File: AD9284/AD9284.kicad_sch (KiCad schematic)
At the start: 0 parts

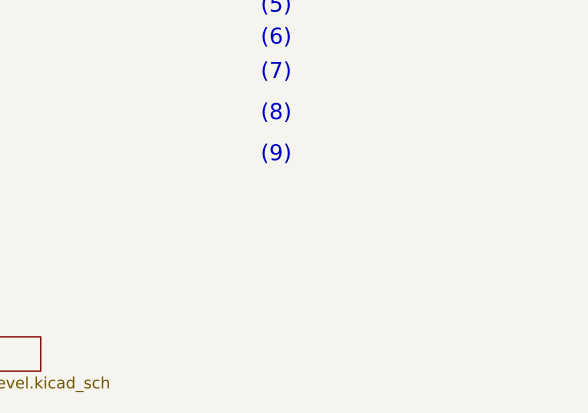
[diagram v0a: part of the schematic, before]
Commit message: Schematic and PCB complete. TODO: BOM
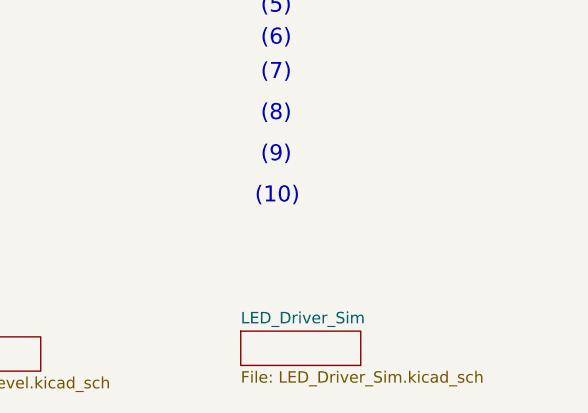
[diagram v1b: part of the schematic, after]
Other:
- added sheet LED_Driver_Sim (LED_Driver_Sim.kicad_sch)
- note added: "(10)"
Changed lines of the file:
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@@
+		)
+	)
+	(text "(10)"
+		(exclude_from_sim no)
+		(at 193.294 120.904 0)
+		(effects
+			(font
+				(size 1.778 1.778)
+			)
+			(href "#10")
 		)
 	)
@@
 		)
 		(column_widths 6.35 86.995 17.399)
-		(row_heights 3.81 3.81 3.81 3.81 3.81 3.81 3.81 4.572 4.572)
+		(row_heights 3.81 3.81 3.81 3.81 3.81 3.81 3.81 4.572 4.572 4.572)
 		(cells
 			(table_cell "1"
@@
 				)
 			)
-			(table_cell "References"
+			(table_cell "LED bjt driver sim"
 				(exclude_from_sim no)
 				(at 97.79 113.792 0)
@@
 				(exclude_from_sim no)
 				(at 184.785 113.792 0)
+				(size 17.399 4.572)
+				(margins 0.9525 0.9525 0.9525 0.9525)
+				(span 1 1)
+				(fill
+					(type none)
+				)
+				(effects
+					(font
+						(size 2.032 2.032)
+					)
+					(justify left top)
+				)
+			)
+			(table_cell "10"
+				(exclude_from_sim no)
+				(at 91.44 118.364 0)
+				(size 6.35 4.572)
+				(margins 0.9525 0.9525 0.9525 0.9525)
+				(span 1 1)
+				(fill
+					(type none)
+				)
+				(effects
+					(font
+						(size 2.032 2.032)
+					)
+					(justify left top)
+				)
+			)
+			(table_cell "References"
+				(exclude_from_sim no)
+				(at 97.79 118.364 0)
+				(size 86.995 4.572)
+				(margins 0.9525 0.9525 0.9525 0.9525)
+				(span 1 1)
+				(fill
+					(type none)
+				)
+				(effects
+					(font
+						(size 2.032 2.032)
+					)
+					(justify left top)
+				)
+			)
+			(table_cell ""
+				(exclude_from_sim no)
+				(at 184.785 118.364 0)
 				(size 17.399 4.572)
 				(margins 0.9525 0.9525 0.9525 0.9525)
@@
 			(effects
 				(font
+					(size 1.27 1.27)
+				)
+				(justify left top)
+			)
+		)
+		(instances
+			(project "AD9284"
+				(path "/d7c6bdb5-efe4-402d-982f-a101ad564d95"
+					(page "10")
+				)
+			)
+		)
+	)
+	(sheet
+		(at 189.23 135.89)
+		(size 13.335 3.81)
+		(exclude_from_sim no)
+		(in_bom yes)
+		(on_board yes)
+		(dnp no)
+		(fields_autoplaced yes)
+		(stroke
+			(width 0.1524)
+			(type solid)
+		)
+		(fill
+			(color 0 0 0 0.0000)
+		)
+		(property "Sheetname" "LED_Driver_Sim"
+			(at 189.23 135.1784 0)
+			(effects
+				(font
+					(size 1.27 1.27)
+				)
+				(justify left bottom)
+			)
+		)
+		(property "Sheetfile" "LED_Driver_Sim.kicad_sch"
+			(at 189.23 140.2846 0)
+			(effects
+				(font
